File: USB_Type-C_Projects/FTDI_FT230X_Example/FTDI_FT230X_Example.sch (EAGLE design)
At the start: 52 parts, among them J1 105450-0101, J2 MF-CON-2.54mm-01x03, J3 MF-CON-2.54mm-01x02, J4 MF-CON-2.54mm-01x05, J5 MF-CON-2.54mm-01x03, J6 MF-CON-2.54mm-01x05, U1 FT230XQ-R, U2 IP4234CZ6,125, U3 IRLML6401TRPBF, U4 NCP1117LPST33T3G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

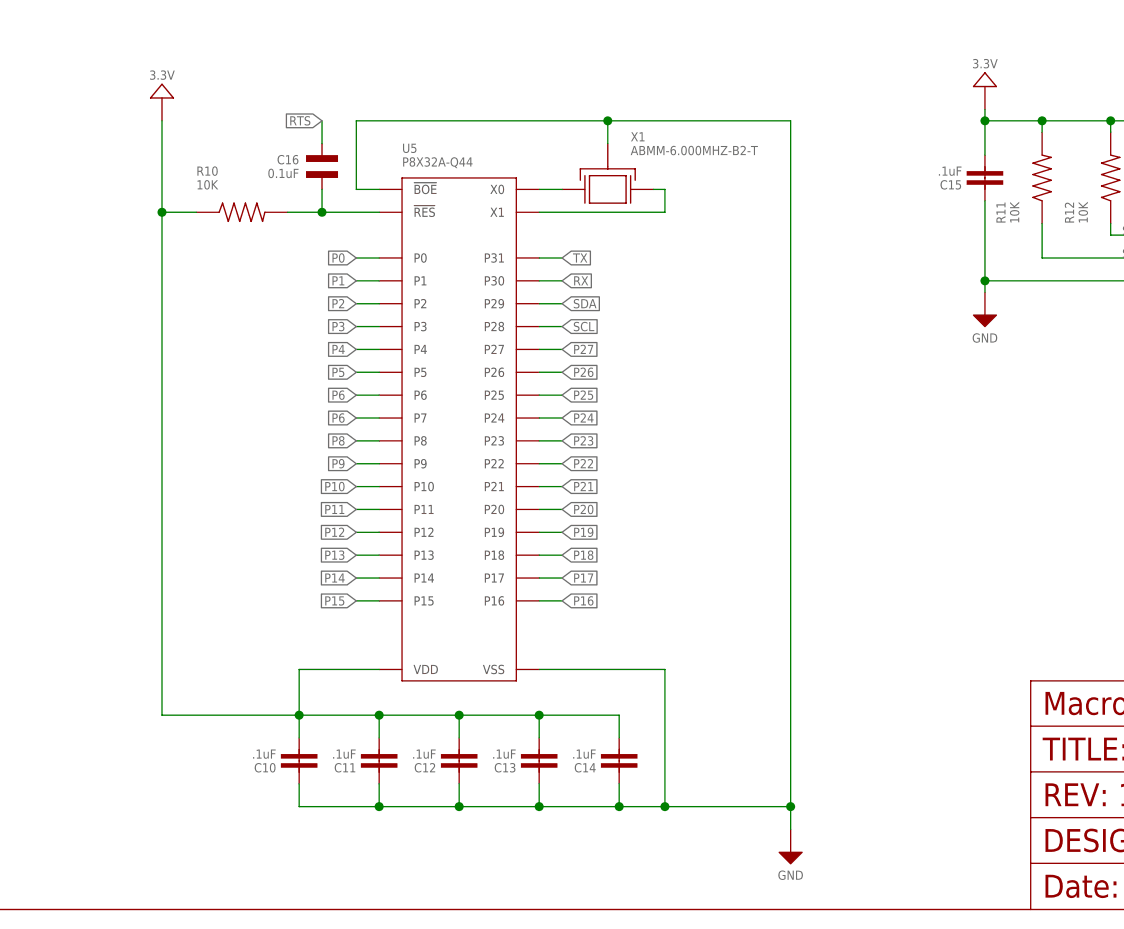
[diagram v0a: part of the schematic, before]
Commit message: Added MPNs and normalized part values
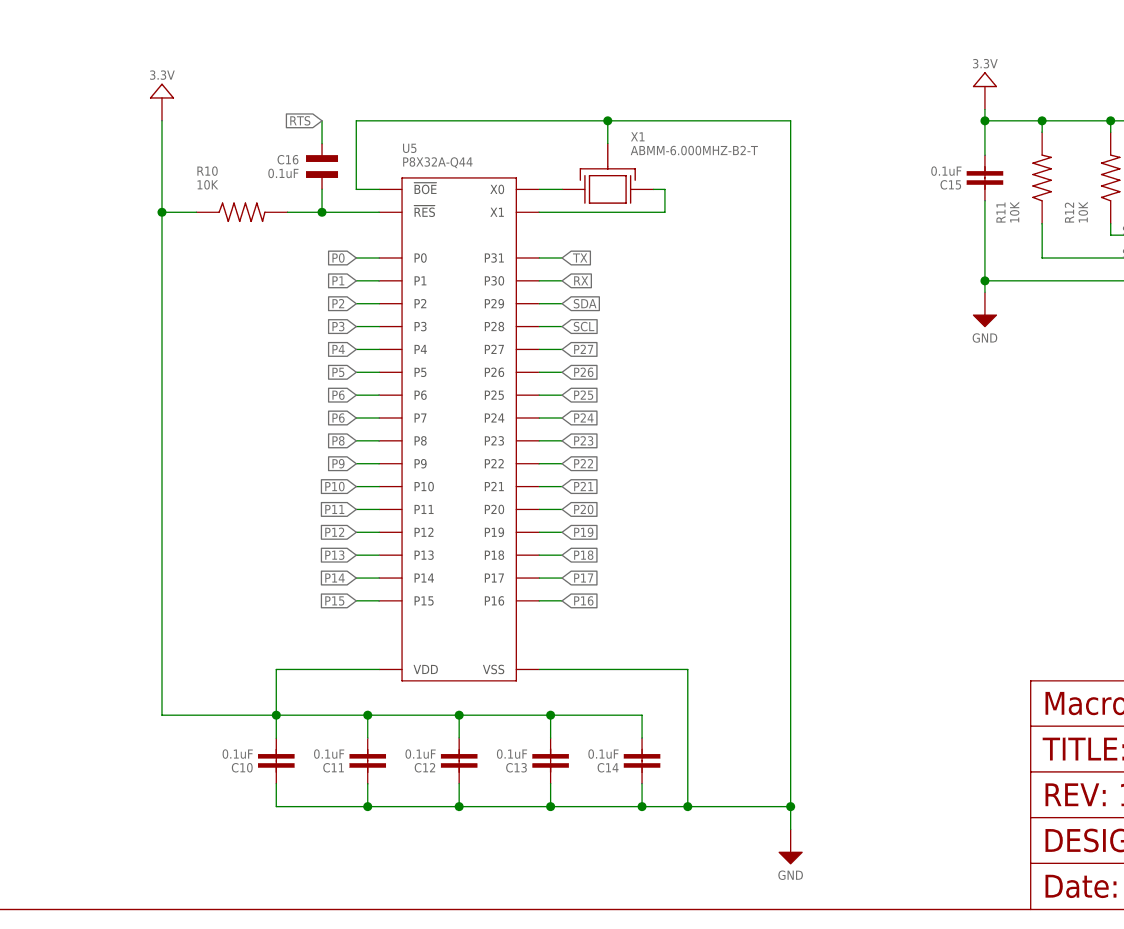
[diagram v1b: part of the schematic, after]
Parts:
- C1: HOUSEPART (none) -> MF-CAP-0603-1uF
- C10, C11, C12, C13, C14, C15: value .1uF -> 0.1uF; MPN (none) -> MF-CAP-0603-0.1uF
- C16, C2, C5, C7, C8: MPN (none) -> MF-CAP-0603-0.1uF
- C3, C4: MPN (none) -> C0603C470J1GACTU
- C6: HOUSEPART (none) -> MF-CAP-1206-10uF
- C9: MPN (none) -> MF-CAP-1206-10uF
- J1: MPN (none) -> 105450-0101
- L1, L2: MPN (none) -> MI0603K300R-10
- R1: MPN (none) -> ERJ-3EKF5101V
- R10, R11, R12: MPN (none) -> MF-RES-0603-10K
- R2, R3: MPN (none) -> MF-RES-0603-27
- R4: MPN (none) -> MF-RES-0603-100K
- R5: MPN (none) -> MF-RES-0603-1K
- R6, R7, R8: MPN (none) -> MF-RES-0603-330
- R9: MPN (none) -> ERJ-3EKF1500V
- TP1, TP2, TP3, TP4: MPN (none) -> 5115
- U1: MPN (none) -> FT230XQ-R
- U2: MPN (none) -> IP4234CZ6,125
- U3: MPN (none) -> IRLML6401TRPBF
- U5: MPN (none) -> P8X32A-Q44
- U6: MPN (none) -> CAT24C512WI-GT3
- X1: MPN (none) -> ABMM-6.000MHZ-B2-T
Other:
- moved on the sheet: C10, C11, C13, C14

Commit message: Forgot a MPN :)
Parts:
- C1: HOUSEPART MF-CAP-0603-1uF -> (none); MPN (none) -> MF-CAP-0603-1uF
- C6: HOUSEPART MF-CAP-1206-10uF -> (none); MPN (none) -> MF-CAP-1206-10uF
- TP1, TP2, TP3, TP4: MPN 5115 -> Keystone 5115
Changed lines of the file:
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@@
 <part name="U$5" library="MF_Aesthetics" deviceset="POWER_RAIL" device="" value="3.3V"/>
 <part name="C6" library="MF_Passives" deviceset="CAPACITOR_NP" device="_1206" value="10uF">
-<attribute name="HOUSEPART" value="MF-CAP-1206-10uF"/>
+<attribute name="MPN" value="MF-CAP-1206-10uF"/>
 </part>
 <part name="C7" library="MF_Passives" deviceset="CAPACITOR_NP" device="_0603" value="0.1uF">
@@
 </part>
 <part name="C1" library="MF_Passives" deviceset="CAPACITOR_NP" device="_0603" value="1uF">
-<attribute name="HOUSEPART" value="MF-CAP-0603-1uF"/>
+<attribute name="MPN" value="MF-CAP-0603-1uF"/>
 </part>
 <part name="C3" library="MF_Passives" deviceset="CAPACITOR_NP" device="_0603" value="47pF">
@@
 </part>
 <part name="TP2" library="PP_Connectors" deviceset="TEST_POINT_SINGLE" device="_KEYSTONE_5115-5119" value="5115">
-<attribute name="MPN" value="5115"/>
+<attribute name="MPN" value="Keystone 5115"/>
 </part>
 <part name="TP3" library="PP_Connectors" deviceset="TEST_POINT_SINGLE" device="_KEYSTONE_5115-5119" value="5115">
-<attribute name="MPN" value="5115"/>
+<attribute name="MPN" value="Keystone 5115"/>
 </part>
 <part name="TP1" library="PP_Connectors" deviceset="TEST_POINT_SINGLE" device="_KEYSTONE_5115-5119" value="5115">
-<attribute name="MPN" value="5115"/>
+<attribute name="MPN" value="Keystone 5115"/>
 </part>
 <part name="J1" library="PP_Connectors" deviceset="USB_TYPE-C" device="_105450-0101" value="105450-0101">
@@
 </part>
 <part name="TP4" library="PP_Connectors" deviceset="TEST_POINT_SINGLE" device="_KEYSTONE_5115-5119" value="5115">
-<attribute name="MPN" value="5115"/>
+<attribute name="MPN" value="Keystone 5115"/>
 </part>
 <part name="J2" library="MF_Connectors" deviceset="CON_01X03" device="_PTH_2.54MM" value="MF-CON-2.54mm-01x03">

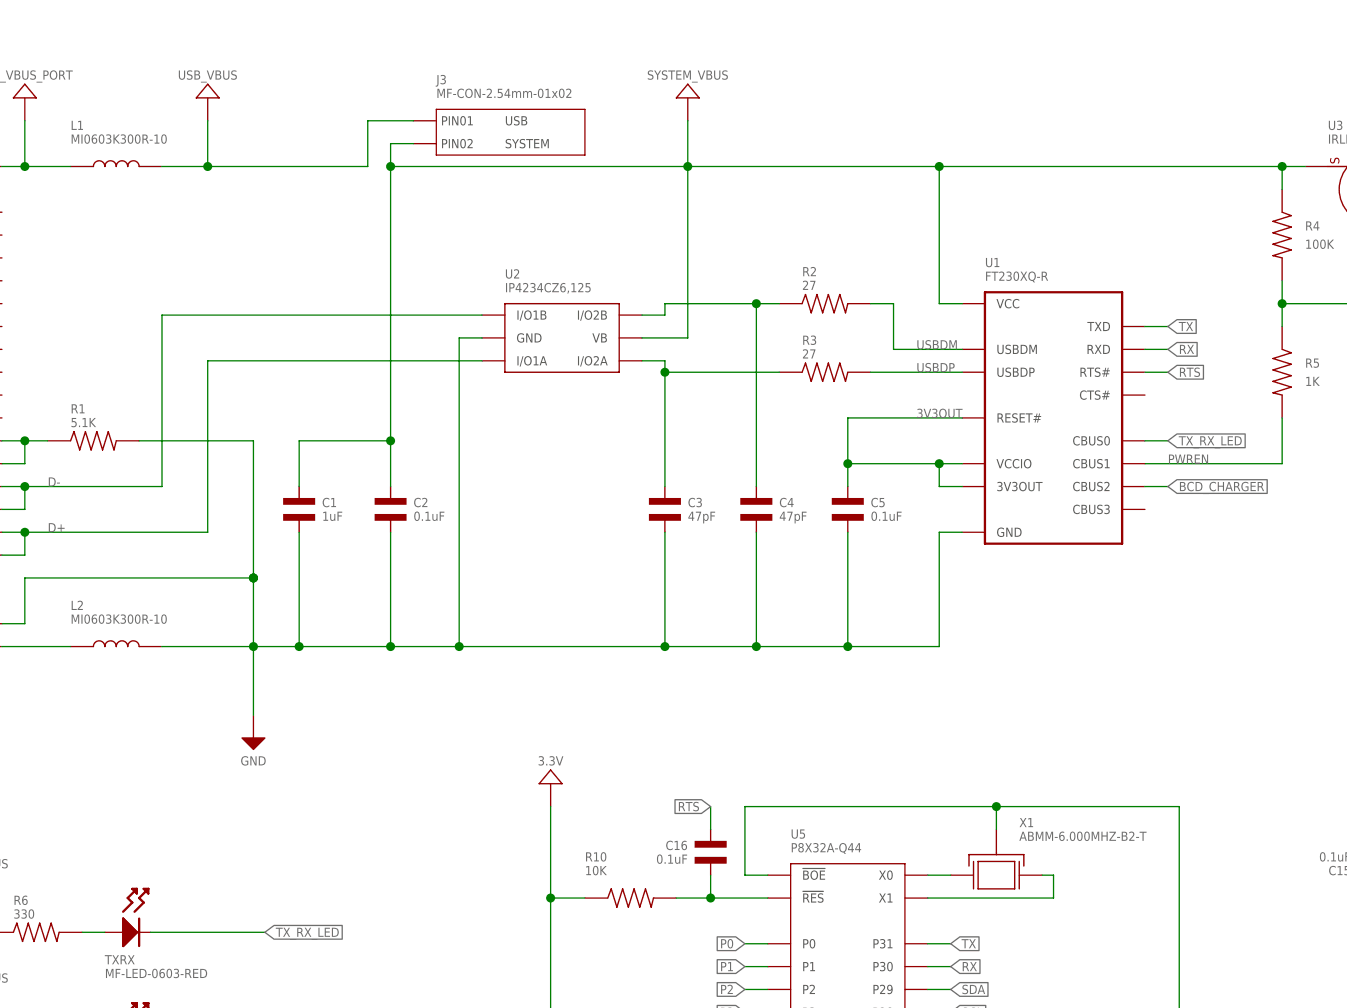
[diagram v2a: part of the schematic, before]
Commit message: Fixed IP4234CZ6 ESD protection
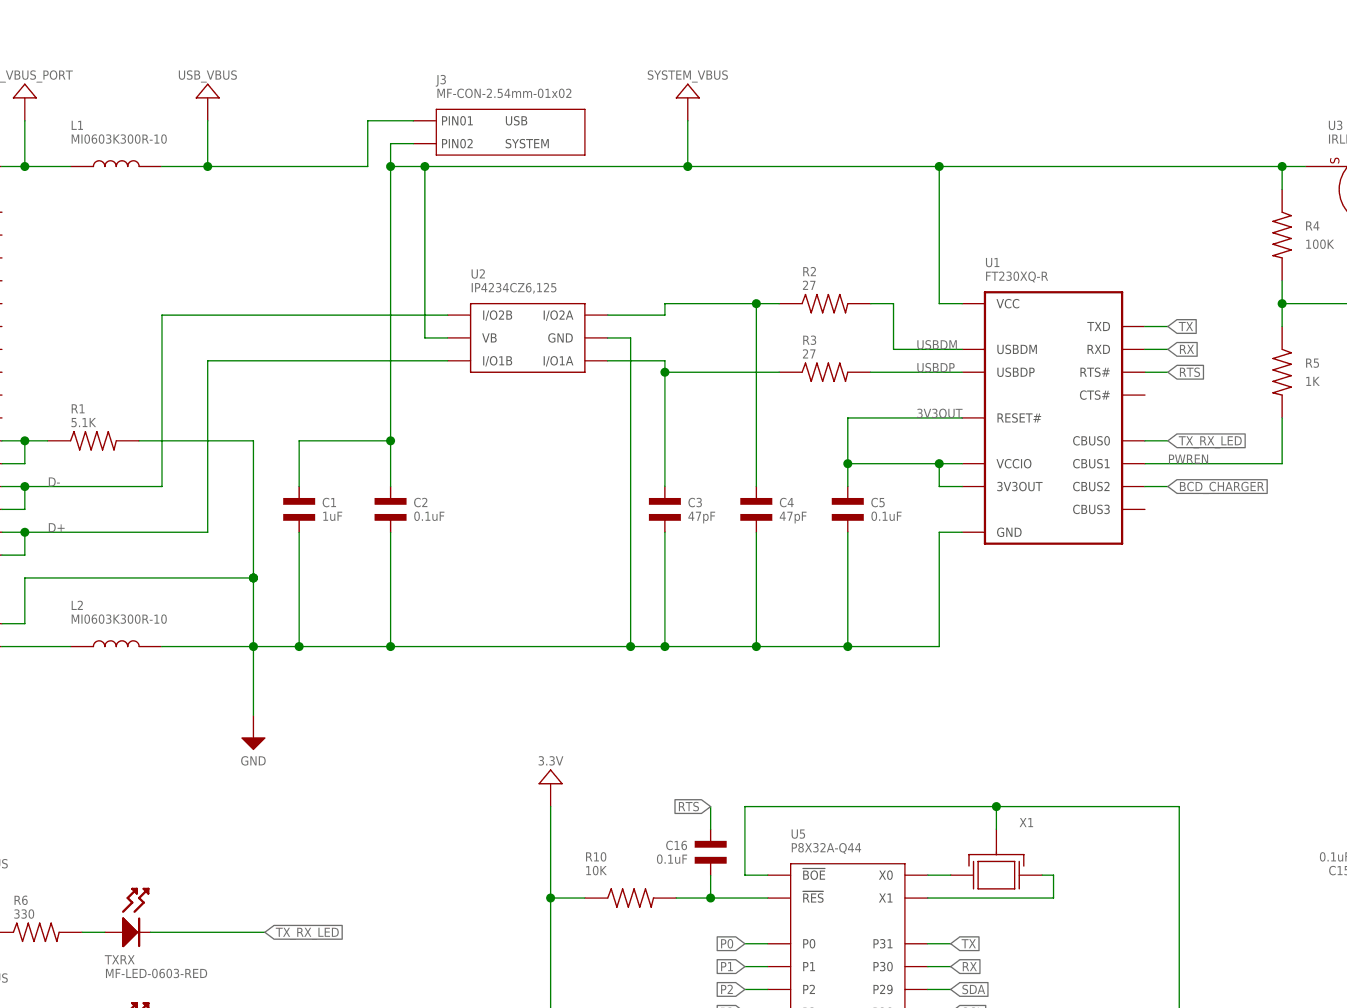
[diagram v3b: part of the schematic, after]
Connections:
- net D+: now also U2.I/O1B; no longer U2.I/O1A
- net D-: now also U2.I/O2B; no longer U2.I/O1B
- net N$14: now also U2.I/O1A; no longer U2.I/O2A
- net N$15: now also U2.I/O2A; no longer U2.I/O2B
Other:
- moved on the sheet: U2
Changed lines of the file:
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@@
 <?xml version="1.0" encoding="utf-8"?>
 <!DOCTYPE eagle SYSTEM "eagle.dtd">
-<eagle version="9.2.2">
+<eagle version="9.3.0">
 <drawing>
 <settings>
@@
 <instance part="X1" gate="G$1" x="134.62" y="80.01" smashed="yes" rot="R180">
 <attribute name="NAME" x="137.16" y="86.36" size="1.016" layer="95" font="vector" align="top-left"/>
-<attribute name="VALUE" x="137.16" y="83.82" size="1.016" layer="96" font="vector"/>
 </instance>
 <instance part="U$5" gate="G$1" x="273.05" y="166.37" smashed="yes">
@@
 <attribute name="VALUE" x="53.34" y="27.94" size="1.016" layer="96" font="vector" rot="R180" align="center"/>
 </instance>
-<instance part="U2" gate="G$1" x="80.01" y="137.16" smashed="yes" rot="MR180">
-<attribute name="NAME" x="80.01" y="147.32" size="1.016" layer="95" font="vector" align="top-left"/>
-<attribute name="VALUE" x="80.01" y="144.78" size="1.016" layer="96" font="vector"/>
-<attribute name="MPN" x="80.01" y="137.16" size="1.778" layer="96" rot="MR180" display="off"/>
+<instance part="U2" gate="G$1" x="88.9" y="137.16" smashed="yes" rot="R180">
+<attribute name="NAME" x="76.2" y="147.32" size="1.016" layer="95" font="vector" align="top-left"/>
+<attribute name="VALUE" x="76.2" y="144.78" size="1.016" layer="96" font="vector"/>
+<attribute name="MPN" x="88.9" y="137.16" size="1.778" layer="96" rot="R180" display="off"/>
 </instance>
 <instance part="U$1" gate="G$1" x="232.41" y="166.37" smashed="yes">
@@
 <wire x1="52.07" y1="97.79" x2="52.07" y2="105.41" width="0.1524" layer="91"/>
 <wire x1="57.15" y1="105.41" x2="67.31" y2="105.41" width="0.1524" layer="91"/>
-<wire x1="67.31" y1="105.41" x2="74.93" y2="105.41" width="0.1524" layer="91"/>
-<wire x1="74.93" y1="105.41" x2="97.79" y2="105.41" width="0.1524" layer="91"/>
+<wire x1="67.31" y1="105.41" x2="93.98" y2="105.41" width="0.1524" layer="91"/>
+<wire x1="93.98" y1="105.41" x2="97.79" y2="105.41" width="0.1524" layer="91"/>
 <wire x1="97.79" y1="105.41" x2="107.95" y2="105.41" width="0.1524" layer="91"/>
 <wire x1="107.95" y1="105.41" x2="118.11" y2="105.41" width="0.1524" layer="91"/>
@@
 <pinref part="L2" gate="G$1" pin="P$2"/>
 <pinref part="U2" gate="G$1" pin="GND"/>
-<wire x1="77.47" y1="139.7" x2="74.93" y2="139.7" width="0.1524" layer="91"/>
-<wire x1="74.93" y1="139.7" x2="74.93" y2="105.41" width="0.1524" layer="91"/>
-<junction x="74.93" y="105.41"/>
+<wire x1="91.44" y1="139.7" x2="93.98" y2="139.7" width="0.1524" layer="91"/>
+<wire x1="93.98" y1="139.7" x2="93.98" y2="105.41" width="0.1524" layer="91"/>
+<junction x="93.98" y="105.41"/>
 </segment>
 <segment>
@@
 <wire x1="26.67" y1="115.57" x2="24.13" y2="115.57" width="0.1524" layer="91"/>
 <junction x="26.67" y="118.11"/>
-<pinref part="U2" gate="G$1" pin="I/O1A"/>
-<wire x1="46.99" y1="137.16" x2="77.47" y2="137.16" width="0.1524" layer="91"/>
+<pinref part="U2" gate="G$1" pin="I/O1B"/>
+<wire x1="46.99" y1="137.16" x2="73.66" y2="137.16" width="0.1524" layer="91"/>
 </segment>
 </net>
@@
 <wire x1="26.67" y1="120.65" x2="24.13" y2="120.65" width="0.1524" layer="91"/>
 <junction x="26.67" y="123.19"/>
-<pinref part="U2" gate="G$1" pin="I/O1B"/>
-<wire x1="41.91" y1="142.24" x2="77.47" y2="142.24" width="0.1524" layer="91"/>
+<pinref part="U2" gate="G$1" pin="I/O2B"/>
+<wire x1="73.66" y1="142.24" x2="41.91" y2="142.24" width="0.1524" layer="91"/>
 </segment>
 </net>
@@
 <pinref part="C3" gate="G$1" pin="P$1"/>
 <wire x1="97.79" y1="123.19" x2="97.79" y2="135.89" width="0.1524" layer="91"/>
-<pinref part="U2" gate="G$1" pin="I/O2A"/>
-<wire x1="95.25" y1="137.16" x2="97.79" y2="137.16" width="0.1524" layer="91"/>
 <wire x1="97.79" y1="137.16" x2="97.79" y2="135.89" width="0.1524" layer="91"/>
 <junction x="97.79" y="135.89"/>
+<pinref part="U2" gate="G$1" pin="I/O1A"/>
+<wire x1="97.79" y1="137.16" x2="91.44" y2="137.16" width="0.1524" layer="91"/>
 </segment>
 </net>
@@
 <wire x1="97.79" y1="143.51" x2="107.95" y2="143.51" width="0.1524" layer="91"/>
 <junction x="107.95" y="143.51"/>
-<pinref part="U2" gate="G$1" pin="I/O2B"/>
-<wire x1="95.25" y1="142.24" x2="97.79" y2="142.24" width="0.1524" layer="91"/>
 <wire x1="97.79" y1="142.24" x2="97.79" y2="143.51" width="0.1524" layer="91"/>
+<pinref part="U2" gate="G$1" pin="I/O2A"/>
+<wire x1="97.79" y1="142.24" x2="91.44" y2="142.24" width="0.1524" layer="91"/>
 </segment>
 </net>
@@
 <junction x="166.37" y="158.75"/>
 <pinref part="R4" gate="G$1" pin="P$1"/>
-<pinref part="U2" gate="G$1" pin="VB"/>
-<wire x1="95.25" y1="139.7" x2="100.33" y2="139.7" width="0.1524" layer="91"/>
-<wire x1="100.33" y1="139.7" x2="100.33" y2="158.75" width="0.1524" layer="91"/>
 <junction x="100.33" y="158.75"/>
 <pinref part="U$3" gate="G$1" pin="P$1"/>
@@
 <wire x1="69.85" y1="161.29" x2="67.31" y2="161.29" width="0.1524" layer="91"/>
 <wire x1="67.31" y1="161.29" x2="67.31" y2="158.75" width="0.1524" layer="91"/>
-<wire x1="67.31" y1="158.75" x2="100.33" y2="158.75" width="0.1524" layer="91"/>
+<wire x1="67.31" y1="158.75" x2="71.12" y2="158.75" width="0.1524" layer="91"/>
 <pinref part="C1" gate="G$1" pin="P$1"/>
 <pinref part="C2" gate="G$1" pin="P$1"/>
+<wire x1="71.12" y1="158.75" x2="100.33" y2="158.75" width="0.1524" layer="91"/>
 <wire x1="67.31" y1="123.19" x2="67.31" y2="128.27" width="0.1524" layer="91"/>
 <wire x1="67.31" y1="128.27" x2="57.15" y2="128.27" width="0.1524" layer="91"/>
@@
 <junction x="67.31" y="128.27"/>
 <junction x="67.31" y="158.75"/>
-</segment>
-<segment>
+<pinref part="U2" gate="G$1" pin="VB"/>
+<wire x1="73.66" y1="139.7" x2="71.12" y2="139.7" width="0.1524" layer="91"/>
+<wire x1="71.12" y1="139.7" x2="71.12" y2="158.75" width="0.1524" layer="91"/>
+<junction x="71.12" y="158.75"/>
+</segment>
+<segment>

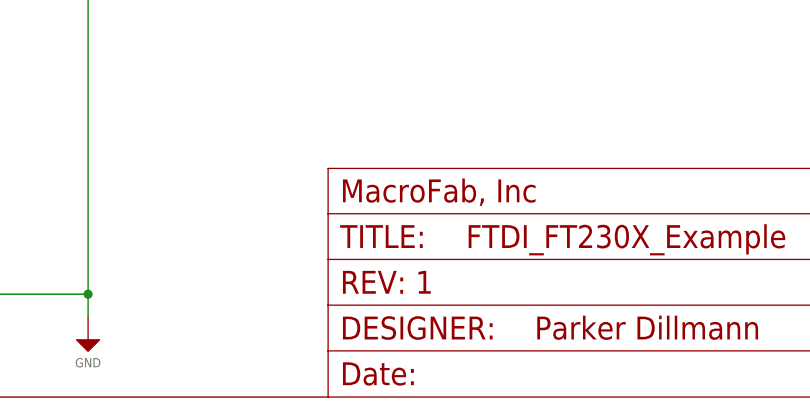
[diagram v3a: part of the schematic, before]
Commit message: REV 2. Fixed USB ESD protection.
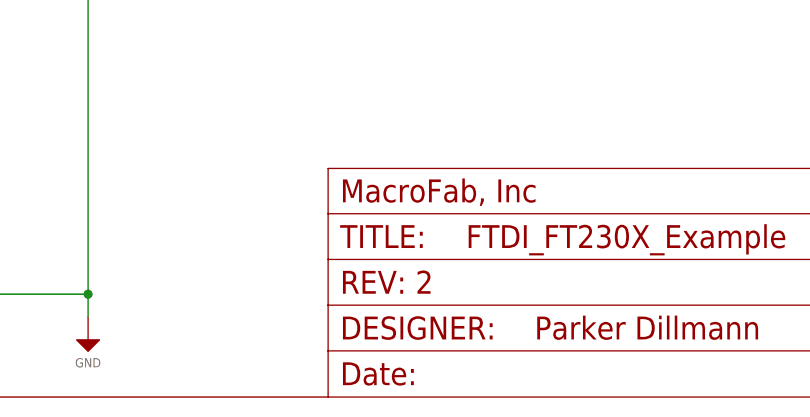
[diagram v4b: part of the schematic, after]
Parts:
- FRAME1: REVNUM REV: 1 -> REV: 2
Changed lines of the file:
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@@
 <?xml version="1.0" encoding="utf-8"?>
 <!DOCTYPE eagle SYSTEM "eagle.dtd">
-<eagle version="9.3.0">
+<eagle version="9.3.2">
 <drawing>
 <settings>
@@
 <part name="FRAME1" library="MF_Aesthetics" deviceset="MF_FRAME" device="DEFAULT" value="MF_FRAMEDEFAULT">
 <attribute name="DNAME" value="Parker Dillmann"/>
-<attribute name="REVNUM" value="REV: 1"/>
+<attribute name="REVNUM" value="REV: 2"/>
 </part>
 <part name="X1" library="MF_Frequency_Control" deviceset="CYRSTAL_GND" device="_ABMM" value="ABMM-6.000MHZ-B2-T">
